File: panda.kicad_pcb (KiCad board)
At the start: 2 copper layers, 100 x 125 mm, 192 parts, among them J1 PIN10-13_Breakout, J10 XT60-M, J11 24V_Lockout_Key_Switch, J12 PT_1, J13 PT_4, J14 PT_2, J15 PT_5, J16 PT_3, J17 PT_6, J18 4-Pin Load Cell, J19 5-Pin Load Cell, J20 Ignitor Screw Terminal, J21 Screw_Terminal_01x03, J22 Screw_Terminal_01x02, J3 USB_C_Receptacle_USB2.0_16P, J4 Valve_1_PWR, J5 Valve_4_PWR, J6 Valve_2_PWR, J7 Valve_5_PWR, J8 Valve_3_PWR, J9 Valve_6_PWR, K1 G5Q-1A DC24, K2 G5Q-1A DC24, Q1 BSS138, Q2 BSS138, Q3 BSS138, Q4 BSS138, Q5 BSS138, Q6 BSS138, Q7 BSS138, Q8 BSS138, SW1 PTS636SM43SMTR LFS, SW2 PTS636SM43SMTR LFS, U1 ESP32-S3-WROOM-1, U2 ADS112C04, U3 ADS112C04, U4 ADS112C04, U5 ADS112C04, U6 TPS5430DDA, U7 XC6220B331PR-G, U8 INA187A1

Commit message: Update date
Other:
- board text added: "PANDA Propulsion Actuation and Nominal Data Acquisition V2.0.0 Nov 6th 2025 Noah Warren"
- board text removed: "PANDA Propulsion Actuation and Nominal Data Acquisition V1.1.0 Sep 10 2025 Noah Warren"
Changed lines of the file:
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@@
 			(psa4output no)
 			(plot_black_and_white yes)
+			(plotinvisibletext no)
 			(sketchpadsonfab no)
 			(plotpadnumbers no)
@@
 		)
 	)
-	(gr_text "PANDA\nPropulsion Actuation and Nominal Data Acquisition\nV1.1.0\nSep 10 2025\nNoah Warren"
+	(gr_text "PANDA\nPropulsion Actuation and Nominal Data Acquisition\nV2.0.0\nNov 6th 2025\nNoah Warren"
 		(at 69.75 151.5 0)
 		(layer "F.SilkS")

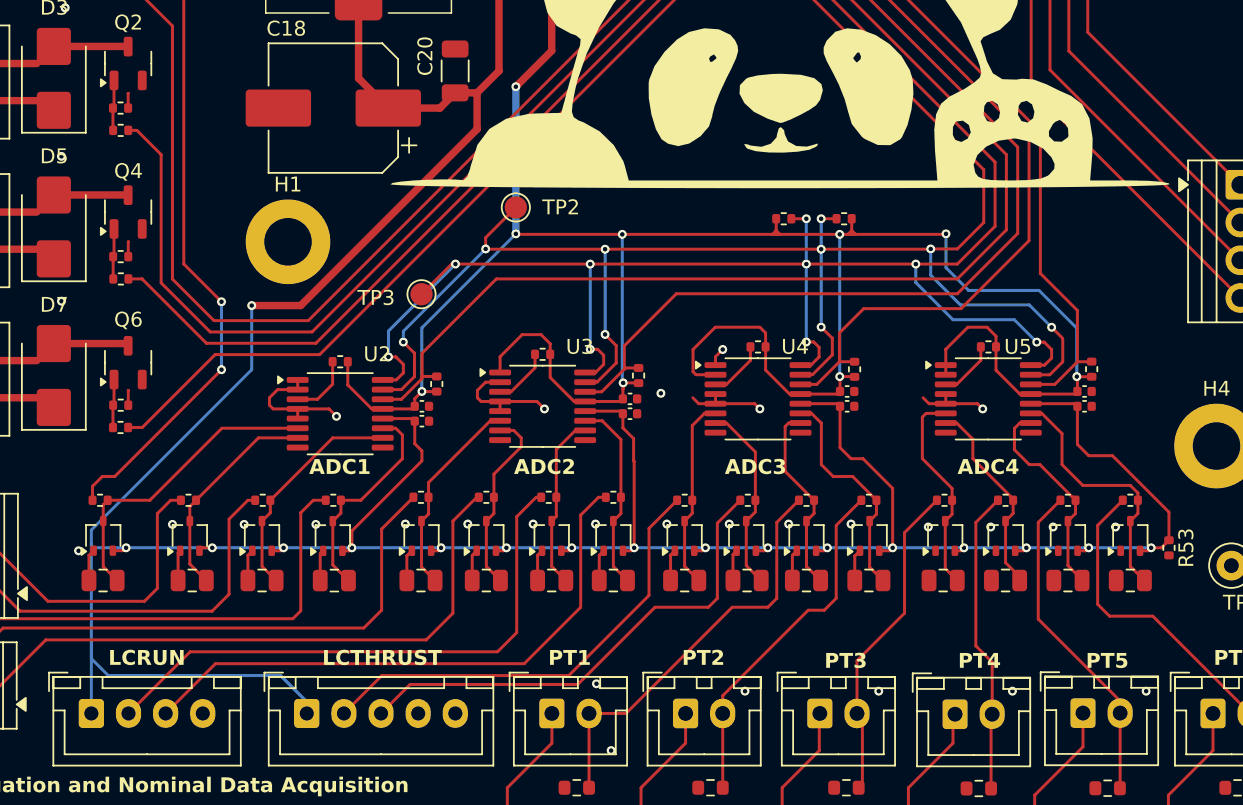
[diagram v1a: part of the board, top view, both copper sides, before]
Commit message: minor fixed + lowered status leds to ~0.6mA, which should give ~50 mcd
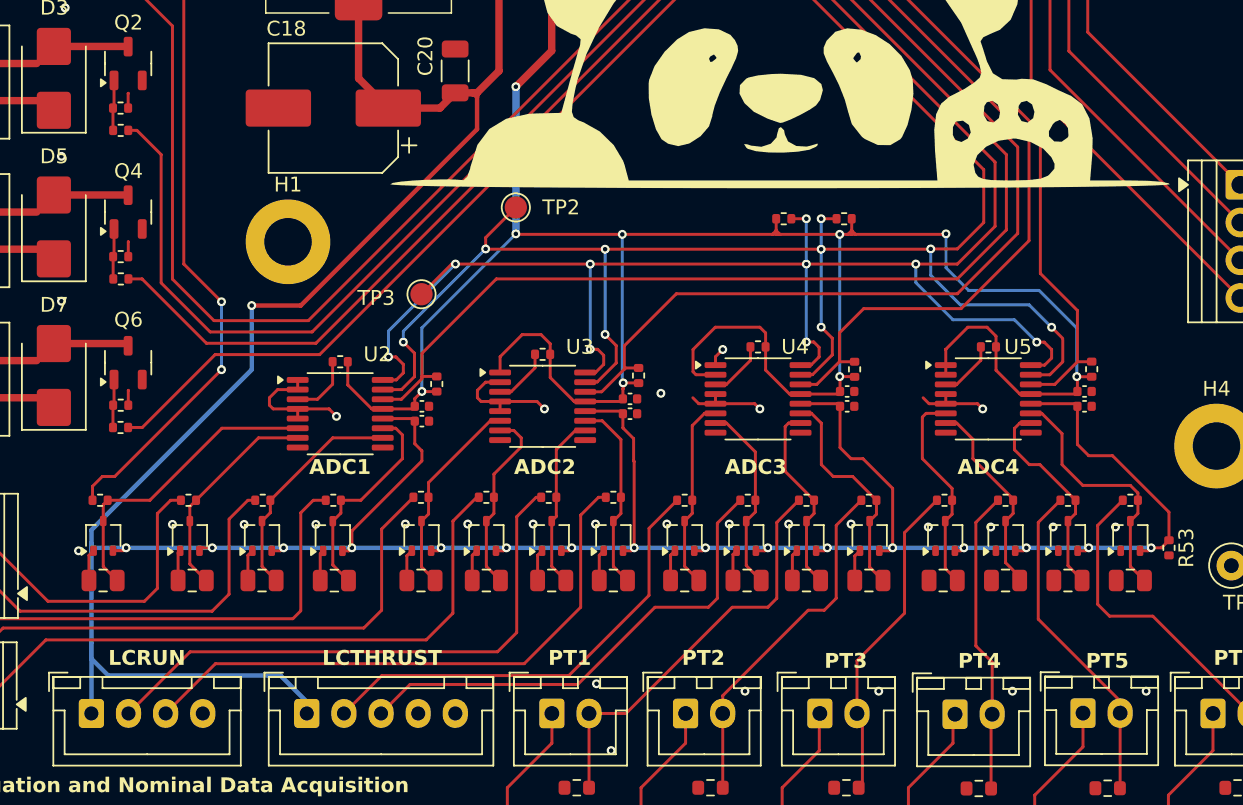
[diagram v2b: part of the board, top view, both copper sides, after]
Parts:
- R29, R32, R33, R50: value 22k -> 39k
- R40: value 1k -> 3.3k
- R8: value 33k -> 39k
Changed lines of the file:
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@@
 			)
 		)
-		(property "Value" "22k"
+		(property "Value" "39k"
 			(at 0 1.17 90)
 			(layer "F.Fab")
@@
 			)
 		)
-		(property "Value" "1k"
+		(property "Value" "3.3k"
 			(at 0 1.17 90)
 			(layer "F.Fab")
@@
 			)
 		)
-		(property "Value" "22k"
+		(property "Value" "39k"
 			(at 0 1.17 90)
 			(layer "F.Fab")
@@
 			)
 		)
-		(property "Value" "22k"
+		(property "Value" "39k"
 			(at 0 1.17 90)
 			(layer "F.Fab")
@@
 			)
 		)
-		(property "Value" "22k"
+		(property "Value" "39k"
 			(at 0 1.17 90)
 			(layer "F.Fab")
@@
 			)
 		)
-		(property "Value" "33k"
+		(property "Value" "39k"
 			(at 0 1.17 0)
 			(layer "F.Fab")
@@
 	)
 	(segment
-		(start 112.5 99.475)
+		(start 113.7 99.475)
 		(end 113.975 99.475)
 		(width 0.5)
@@
 	)
 	(segment
+		(start 112.5 99.475)
+		(end 113.7 99.475)
+		(width 0.5)
+		(layer "F.Cu")
+		(net 3)
+	)
+	(segment
 		(start 105.344221 130.305779)
 		(end 105.55 130.1)
@@
 		(start 102.108 113.792)
 		(end 98.806 113.792)
-		(width 0.5)
+		(width 0.3)
 		(layer "F.Cu")
 		(net 3)
@@
 		(start 113.975 101.925)
 		(end 102.108 113.792)
-		(width 0.5)
+		(width 0.3)
 		(layer "F.Cu")
 		(net 3)
@@
 	)
 	(segment
+		(start 113.975 99.75)
+		(end 113.975 101.925)
+		(width 0.3)
+		(layer "F.Cu")
+		(net 3)
+	)
+	(segment
 		(start 132.5 58.5)
 		(end 132.5 43.141)
@@
 	)
 	(segment
+		(start 113.975 99.75)
+		(end 113.7 99.475)
+		(width 0.3)
+		(layer "F.Cu")
+		(net 3)
+	)
+	(segment
 		(start 158.6 130.3)
 		(end 159.15 130.3)
@@
 	(segment
 		(start 113.975 99.475)
-		(end 113.975 101.925)
-		(width 0.5)
+		(end 113.975 99.75)
+		(width 0.3)
 		(layer "F.Cu")
 		(net 3)
@@
 		(start 100.95 130.1)
 		(end 105.55 130.1)
-		(width 0.2)
+		(width 0.3)
 		(layer "B.Cu")
 		(net 3)
@@
 		(start 88.012501 130.1)
 		(end 88.012501 129.794)
-		(width 0.2)
+		(width 0.3)
 		(layer "B.Cu")
 		(net 3)
@@
 		(start 105.55 130.1)
 		(end 111.55 130.1)
-		(width 0.2)
+		(width 0.3)
 		(layer "B.Cu")
 		(net 3)
@@
 		(start 137.55 130.1)
 		(end 141.95 130.1)
-		(width 0.2)
+		(width 0.3)
 		(layer "B.Cu")
 		(net 3)
@@
 		(start 100.75 138.7)
 		(end 89.15 138.7)
-		(width 0.2)
+		(width 0.3)
 		(layer "B.Cu")
 		(net 3)
@@
 		(start 141.95 130.1)
 		(end 146.75 130.1)
-		(width 0.2)
+		(width 0.3)
 		(layer "B.Cu")
 		(net 3)
@@
 		(start 115.95 130.1)
 		(end 120.35 130.1)
-		(width 0.2)
+		(width 0.3)
 		(layer "B.Cu")
 		(net 3)
@@
 		(start 102.512501 140.462501)
 		(end 100.75 138.7)
-		(width 0.2)
+		(width 0.3)
 		(layer "B.Cu")
 		(net 3)
@@
 		(start 133.55 130.1)
 		(end 137.55 130.1)
-		(width 0.2)
+		(width 0.3)
 		(layer "B.Cu")
 		(net 3)
@@
 		(start 88.012501 129.794)
 		(end 88.012501 129.974501)
-		(width 0.2)
+		(width 0.3)
 		(layer "B.Cu")
 		(net 3)
@@
 		(start 98.806 113.792)
 		(end 98.806 118.11)
-		(width 0.2)
+		(width 0.3)
 		(layer "B.Cu")
 		(net 3)
@@
 		(start 88.012501 136.5)
 		(end 88.012501 141.25)
-		(width 0.2)
+		(width 0.3)
 		(layer "B.Cu")
 		(net 3)
@@
 		(start 90.35 130.1)
 		(end 96.15 130.1)
-		(width 0.2)
+		(width 0.3)
 		(layer "B.Cu")
 		(net 3)
@@
 		(start 150.95 130.1)
 		(end 155.15 130.1)
-		(width 0.2)
+		(width 0.3)
 		(layer "B.Cu")
 		(net 3)
@@
 		(start 96.15 130.1)
 		(end 100.95 130.1)
-		(width 0.2)
+		(width 0.3)
 		(layer "B.Cu")
 		(net 3)
@@
 		(start 88.012501 130.1)
 		(end 88.138 130.1)
-		(width 0.2)
+		(width 0.3)
 		(layer "B.Cu")
 		(net 3)
@@
 		(start 88.012501 128.903499)
 		(end 88.012501 129.794)
-		(width 0.2)
+		(width 0.3)
 		(layer "B.Cu")
 		(net 3)
@@
 		(start 98.806 118.11)
 		(end 88.012501 128.903499)
-		(width 0.2)
+		(width 0.3)
 		(layer "B.Cu")
 		(net 3)
@@
 		(start 89.15 138.7)
 		(end 88.012501 137.562501)
-		(width 0.2)
+		(width 0.3)
 		(layer "B.Cu")
 		(net 3)
@@
 		(start 88.138 130.1)
 		(end 90.35 130.1)
-		(width 0.2)
+		(width 0.3)
 		(layer "B.Cu")
 		(net 3)
@@
 		(start 146.75 130.1)
 		(end 150.95 130.1)
-		(width 0.2)
+		(width 0.3)
 		(layer "B.Cu")
 		(net 3)
@@
 		(start 129.35 130.1)
 		(end 133.55 130.1)
-		(width 0.2)
+		(width 0.3)
 		(layer "B.Cu")
 		(net 3)
@@
 		(start 88.012501 130.1)
 		(end 88.012501 130.302)
-		(width 0.2)
+		(width 0.3)
 		(layer "B.Cu")
 		(net 3)
@@
 		(start 111.55 130.1)
 		(end 115.95 130.1)
-		(width 0.2)
+		(width 0.3)
 		(layer "B.Cu")
 		(net 3)
@@
 		(start 124.55 130.1)
 		(end 129.35 130.1)
-		(width 0.2)
+		(width 0.3)
 		(layer "B.Cu")
 		(net 3)
@@
 		(start 120.35 130.1)
 		(end 124.55 130.1)
-		(width 0.2)
+		(width 0.3)
 		(layer "B.Cu")
 		(net 3)
@@
 		(start 88.012501 130.302)
 		(end 88.012501 136.5)
-		(width 0.2)
+		(width 0.3)
 		(layer "B.Cu")
 		(net 3)
@@
 		(start 88.012501 129.974501)
 		(end 88.138 130.1)
-		(width 0.2)
+		(width 0.3)
 		(layer "B.Cu")
 		(net 3)
@@
 		(start 155.15 130.1)
 		(end 159.35 130.1)
-		(width 0.2)
+		(width 0.3)
 		(layer "B.Cu")
 		(net 3)

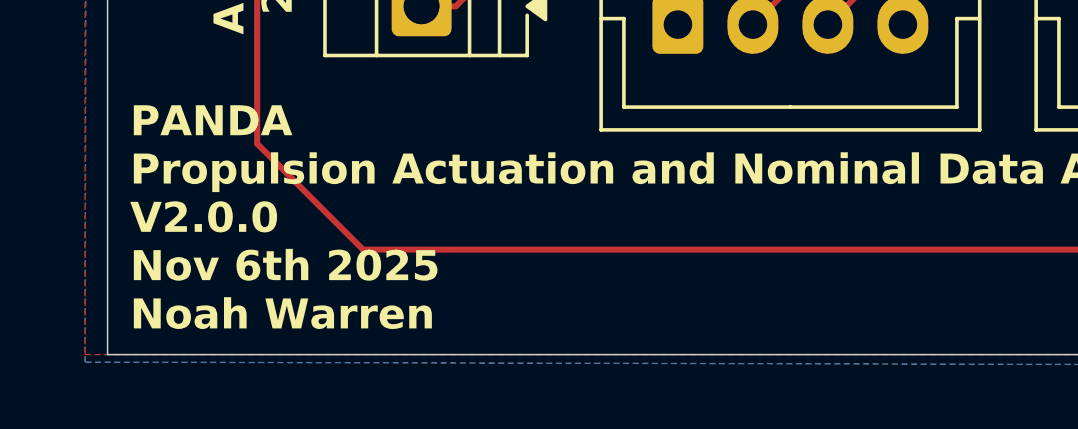
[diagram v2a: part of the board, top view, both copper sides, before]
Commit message: updated name on pcb
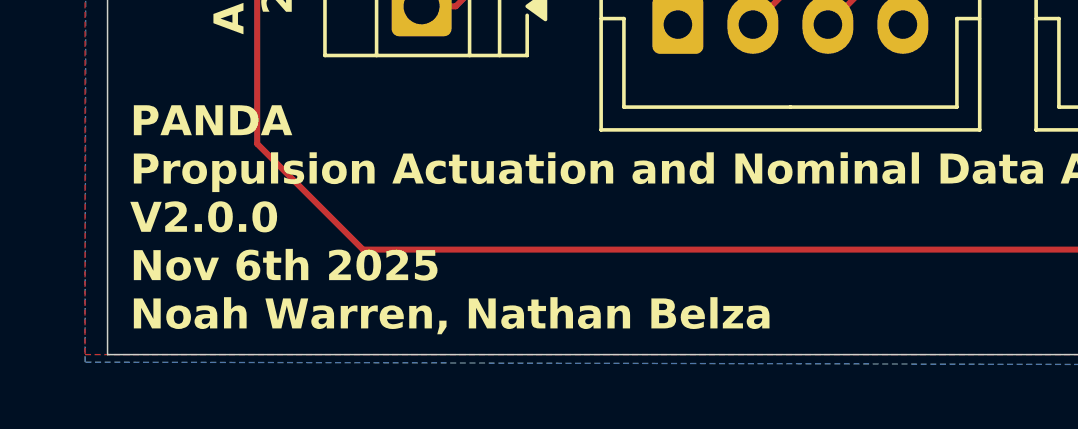
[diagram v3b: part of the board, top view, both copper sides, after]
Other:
- board text added: "PANDA Propulsion Actuation and Nominal Data Acquisition V2.0.0 Nov 6th 2025 Noah Warren, Nathan Belza"
- board text removed: "PANDA Propulsion Actuation and Nominal Data Acquisition V2.0.0 Nov 6th 2025 Noah Warren"
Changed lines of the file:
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@@
 			(psa4output no)
 			(plot_black_and_white yes)
-			(plotinvisibletext no)
 			(sketchpadsonfab no)
 			(plotpadnumbers no)
@@
 		)
 	)
-	(gr_text "PANDA\nPropulsion Actuation and Nominal Data Acquisition\nV2.0.0\nNov 6th 2025\nNoah Warren"
+	(gr_text "PANDA\nPropulsion Actuation and Nominal Data Acquisition\nV2.0.0\nNov 6th 2025\nNoah Warren, Nathan Belza"
 		(at 69.75 151.5 0)
 		(layer "F.SilkS")

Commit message: add capacitor and resistor footprints
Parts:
- removed G***: LOGO, LOGO
- removed J20: Ignitor Screw Terminal, TerminalBlock_4Ucon:TerminalBlock_4Ucon_1x02_P3.50mm_Vertical
- removed J21: Screw_Terminal_01x03, TerminalBlock:TerminalBlock_Xinya_XY308-2.54-3P_1x03_P2.54mm_Horizontal
- removed J22: Screw_Terminal_01x02, TerminalBlock:TerminalBlock_Xinya_XY308-2.54-2P_1x02_P2.54mm_Horizontal
- added C22: 22uF, Capacitor_SMD:C_0805_2012Metric, F.Cu at (100.3, 149.2)
- added C23: 0.1μF, Capacitor_SMD:C_0402_1005Metric, F.Cu at (96.6, 144.1)
- added C40: 0.1μF, Capacitor_SMD:C_0402_1005Metric, F.Cu at (88.6, 167.4)
- added C41: 10nF, Capacitor_SMD:C_0603_1608Metric, F.Cu at (89.1, 155.6)
- added C42: 0.1μF, Capacitor_SMD:C_0402_1005Metric, F.Cu at (159.7, 90.9)
- added C43: 10nF, Capacitor_SMD:C_0603_1608Metric, F.Cu at (89.1, 158.1)
- added C44: 10nF, Capacitor_SMD:C_0603_1608Metric, F.Cu at (89.1, 160.7)
- added C45: 0.1μF, Capacitor_SMD:C_0402_1005Metric, F.Cu at (159.7, 92.9)
- added C46: 10nF, Capacitor_SMD:C_0603_1608Metric, F.Cu at (89.1, 163.2)
- added C47: 0.1μF, Capacitor_SMD:C_0402_1005Metric, F.Cu at (69.0, 165.4)
- added C48: 0.1μF, Capacitor_SMD:C_0402_1005Metric, F.Cu at (69.0, 167.4)
- added C49: 10nF, Capacitor_SMD:C_0603_1608Metric, F.Cu at (69.5, 155.6)
- added C50: 0.1μF, Capacitor_SMD:C_0402_1005Metric, F.Cu at (154.8, 90.9)
- added C51: 10nF, Capacitor_SMD:C_0603_1608Metric, F.Cu at (69.5, 158.1)
- added C52: 10nF, Capacitor_SMD:C_0603_1608Metric, F.Cu at (69.5, 160.7)
- added C53: 0.1μF, Capacitor_SMD:C_0402_1005Metric, F.Cu at (154.8, 92.9)
- added C54: 10nF, Capacitor_SMD:C_0603_1608Metric, F.Cu at (69.5, 163.2)
- added C55: 3.3uF, Capacitor_SMD:C_0805_2012Metric, F.Cu at (33.9, 138.1)
- added C56: 3.3uF, Capacitor_SMD:C_0805_2012Metric, F.Cu at (33.9, 141.1)
- added C57: 3.3uF, Capacitor_SMD:C_0805_2012Metric, F.Cu at (33.9, 144.1)
- added C58: 3.3uF, Capacitor_SMD:C_0805_2012Metric, F.Cu at (33.9, 147.1)
- added C59: 3.3uF, Capacitor_SMD:C_0805_2012Metric, F.Cu at (33.9, 150.1)
- added C60: 3.3uF, Capacitor_SMD:C_0805_2012Metric, F.Cu at (33.9, 153.1)
- added C61: 0.1μF, Capacitor_SMD:C_0402_1005Metric, F.Cu at (98.8, 117.4)
- added C62: 0.1μF, Capacitor_SMD:C_0402_1005Metric, F.Cu at (108.1, 173.9)
- added C63: 0.1μF, Capacitor_SMD:C_0402_1005Metric, F.Cu at (108.1, 175.9)
- added C64: 150nF, Capacitor_SMD:C_0402_1005Metric, F.Cu at (108.1, 177.8)
- added C65: 150nF, Capacitor_SMD:C_0402_1005Metric, F.Cu at (108.1, 179.8)
- added C66: 150nF, Capacitor_SMD:C_0402_1005Metric, F.Cu at (108.1, 181.8)
- added C67: 150nF, Capacitor_SMD:C_0402_1005Metric, F.Cu at (108.1, 183.8)
- added D17: BAT54SW, Package_TO_SOT_SMD:SOT-323_SC-70, F.Cu at (84.9, 156.4)
- added D18: BAT54SW, Package_TO_SOT_SMD:SOT-323_SC-70, F.Cu at (84.9, 160.3)
- added D37: BAT54SW, Package_TO_SOT_SMD:SOT-323_SC-70, F.Cu at (104.5, 186.5)
- added F2: Fuse, Fuse:Fuseholder_Blade_Mini_Keystone_3568, F.Cu at (78.4, 112.3)
- added J2: XT60-M, Connector_AMASS:AMASS_XT60PW-F_1x02_P7.20mm_Horizontal, F.Cu at (34.6, 101.1)
- added K3: G5Q-1 DC24, Relay_THT:Relay_SPDT_Omron-G5Q-1, F.Cu at (77.1, 107.4)
- added Q10: BSS138, Package_TO_SOT_SMD:SOT-23-3, F.Cu at (58.5, 156.6)
- added Q11: BSS138, Package_TO_SOT_SMD:SOT-23-3, F.Cu at (58.5, 161.1)
- added Q9: BSS138, Package_TO_SOT_SMD:SOT-23-3, F.Cu at (58.5, 152.2)
- added R47: Rb, Resistor_SMD:R_0402_1005Metric, F.Cu at (92.6, 164.0)
- added R48: Rb, Resistor_SMD:R_0402_1005Metric, F.Cu at (92.6, 165.9)
- added R70: 250, Resistor_SMD:R_0603_1608Metric, F.Cu at (33.6, 160.9)
- added R71: 250, Resistor_SMD:R_0603_1608Metric, F.Cu at (33.6, 163.4)
- added R72: 10, Resistor_SMD:R_0402_1005Metric, F.Cu at (125.4, 161.1)
- added R73: 10, Resistor_SMD:R_0402_1005Metric, F.Cu at (125.4, 163.1)
- added R74: 250, Resistor_SMD:R_0603_1608Metric, F.Cu at (33.6, 165.9)
- added R75: 250, Resistor_SMD:R_0603_1608Metric, F.Cu at (33.6, 168.4)
- added R76: 39k, Resistor_SMD:R_0402_1005Metric, F.Cu at (98.8, 107.5)
- added R77: 25m 1W, Resistor_SMD:R_1206_3216Metric, F.Cu at (103.0, 117.0)
- added R78: 10k, Resistor_SMD:R_0402_1005Metric, F.Cu at (98.8, 109.4)
- added R79: 10k, Resistor_SMD:R_0402_1005Metric, F.Cu at (98.8, 111.4)
- added R80: 100, Resistor_SMD:R_0402_1005Metric, F.Cu at (98.8, 113.4)
- added R81: 100, Resistor_SMD:R_0402_1005Metric, F.Cu at (98.8, 115.4)
- added R82: 100, Resistor_SMD:R_0402_1005Metric, F.Cu at (49.0, 170.9)
- added R83: 100, Resistor_SMD:R_0402_1005Metric, F.Cu at (49.0, 172.9)
- added R84: 100k, Resistor_SMD:R_0603_1608Metric, F.Cu at (49.0, 174.8)
- added R85: 100k, Resistor_SMD:R_0603_1608Metric, F.Cu at (49.0, 176.8)
- added R86: 100, Resistor_SMD:R_0402_1005Metric, F.Cu at (51.9, 170.9)
- added R87: 100, Resistor_SMD:R_0402_1005Metric, F.Cu at (51.9, 172.9)
- added R88: 100k, Resistor_SMD:R_0603_1608Metric, F.Cu at (51.9, 174.8)
- added R89: 100k, Resistor_SMD:R_0603_1608Metric, F.Cu at (51.9, 176.8)
- added R90: 100, Resistor_SMD:R_0402_1005Metric, F.Cu at (54.8, 170.9)
- added R91: 100, Resistor_SMD:R_0402_1005Metric, F.Cu at (54.8, 172.9)
- added R92: 100k, Resistor_SMD:R_0603_1608Metric, F.Cu at (54.8, 174.8)
- added R93: 100k, Resistor_SMD:R_0603_1608Metric, F.Cu at (54.8, 176.8)
- added R94: 47, Resistor_SMD:R_0402_1005Metric, F.Cu at (111.0, 173.9)
- added R95: 1k, Resistor_SMD:R_0402_1005Metric, F.Cu at (111.0, 175.9)
- added R96: 1k, Resistor_SMD:R_0402_1005Metric, F.Cu at (111.0, 177.9)
- added R97: 1k, Resistor_SMD:R_0402_1005Metric, F.Cu at (111.0, 179.9)
- added R98: 10k, Resistor_SMD:R_0402_1005Metric, F.Cu at (111.0, 181.9)
- added U10: ADS112C04, Package_SO:TSSOP-16_4.4x5mm_P0.65mm, F.Cu at (95.9, 157.7)
- added U11: ADS112C04, Package_SO:TSSOP-16_4.4x5mm_P0.65mm, F.Cu at (76.3, 157.7)
- added U12: INA187A1, Package_TO_SOT_SMD:SOT-23-6, F.Cu at (94.8, 112.2)
- added U13: ADS112C04, Package_SO:TSSOP-16_4.4x5mm_P0.65mm, F.Cu at (114.3, 186.2)
- added U9: ADS112C04, Package_SO:TSSOP-16_4.4x5mm_P0.65mm, F.Cu at (115.5, 105.2)
- C1: value 22uF -> 0.1μF; footprint Capacitor_SMD:C_1206_3216Metric -> Capacitor_SMD:C_0402_1005Metric
- C10, C12: value 0.1μF -> 22uF; footprint Capacitor_SMD:C_0402_1005Metric -> Capacitor_SMD:C_0805_2012Metric
- C11: value 0.1μF -> 10nF
- C13, C8: value 0.1μF -> 10uF; footprint Capacitor_SMD:C_0402_1005Metric -> Capacitor_SMD:C_0805_2012Metric
- C14, C15: value 10uF -> 0.1μF; footprint Capacitor_SMD:C_1206_3216Metric -> Capacitor_SMD:C_0402_1005Metric
- C16: value 10nF -> 2.2uF; footprint Capacitor_SMD:C_0402_1005Metric -> Capacitor_SMD:C_0603_1608Metric
- C17, C20: footprint Capacitor_SMD:C_1206_3216Metric -> Capacitor_SMD:C_0805_2012Metric
- C18: value 220uF -> 0.1μF; footprint Capacitor_SMD:CP_Elec_8x10.5 -> Capacitor_SMD:C_0402_1005Metric
- C2: value 0.1μF -> 100uF; footprint Capacitor_SMD:C_0402_1005Metric -> Capacitor_SMD:CP_Elec_10x10
- C24: value 68nF -> 1uF; footprint Capacitor_SMD:C_0805_2012Metric -> Capacitor_SMD:C_0603_1608Metric
- C25, C26, C27, C28, C33, C34, C39: value 68nF -> 0.1μF; footprint Capacitor_SMD:C_0805_2012Metric -> Capacitor_SMD:C_0402_1005Metric
- C29, C30, C31, C32, C35, C36, C37, C38: value 68nF -> 150nF; footprint Capacitor_SMD:C_0805_2012Metric -> Capacitor_SMD:C_0402_1005Metric
- C3: value 0.1μF -> 10uF; footprint Capacitor_SMD:C_0402_1005Metric -> Capacitor_SMD:C_1206_3216Metric
- C4: value 1μF -> 10uF; footprint Capacitor_SMD:C_0402_1005Metric -> Capacitor_SMD:C_1206_3216Metric
- C5: value 0.1uF -> 220nF; footprint Capacitor_SMD:C_0402_1005Metric -> Capacitor_SMD:C_0805_2012Metric
- C6: value 0.1μF -> 1uF; footprint Capacitor_SMD:C_0402_1005Metric -> Capacitor_SMD:C_0603_1608Metric
- C9: value 0.1μF -> 3pF; footprint Capacitor_SMD:C_0402_1005Metric -> Capacitor_SMD:C_0603_1608Metric
- D1: value LED-Y -> LED-G
- D10, D15, D16, D19, D9: value LED-G -> BAT54SW; footprint LED_SMD:LED_0805_2012Metric -> Package_TO_SOT_SMD:SOT-323_SC-70
- D11, D14, D20: value SK44BL -> BAT54SW; footprint Diode_SMD:D_SMB -> Package_TO_SOT_SMD:SOT-323_SC-70
- D12, D13: value 1N5819HW-7-F -> BAT54SW; footprint Diode_SMD:D_SOD-123 -> Package_TO_SOT_SMD:SOT-323_SC-70
- D2: value SK44BL -> SMCJ26A-13-F; footprint Diode_SMD:D_SMB -> Diode_SMD:D_SMC
- D25: value BAT54SW -> LED-G; footprint Package_TO_SOT_SMD:SOT-323_SC-70 -> LED_SMD:LED_0805_2012Metric
- D26, D27, D28, D29, D30, D31, D32, D33: value BAT54SW -> SK44BL; footprint Package_TO_SOT_SMD:SOT-323_SC-70 -> Diode_SMD:D_SMB
- D3, D4, D6, D7: value SK44BL -> LED-G; footprint Diode_SMD:D_SMB -> LED_SMD:LED_0805_2012Metric
- D8: value LED-G -> LED-Y
- J1: value PIN10-13_Breakout -> Logic_Power_Switch; footprint TerminalBlock:TerminalBlock_Xinya_XY308-2.54-4P_1x04_P2.54mm_Horizontal -> Connector_JST:JST_XH_B2B-XH-A_1x02_P2.50mm_Vertical
- J10: value XT60-M -> PT_6; footprint Connector_AMASS:AMASS_XT60PW-F_1x02_P7.20mm_Horizontal -> Connector_JST:JST_XH_B2B-XH-A_1x02_P2.50mm_Vertical
- J11: value 24V_Lockout_Key_Switch -> 4-Pin Load Cell; footprint Connector_JST:JST_XH_B2B-XH-A_1x02_P2.50mm_Vertical -> Connector_JST:JST_XH_B4B-XH-A_1x04_P2.50mm_Vertical
- J12: value PT_1 -> 5-Pin Load Cell; footprint Connector_JST:JST_XH_B2B-XH-A_1x02_P2.50mm_Vertical -> Connector_JST:JST_XH_B5B-XH-A_1x05_P2.50mm_Vertical
- J13: value PT_4 -> Ignitor Screw Terminal; footprint Connector_JST:JST_XH_B2B-XH-A_1x02_P2.50mm_Vertical -> TerminalBlock_4Ucon:TerminalBlock_4Ucon_1x02_P3.50mm_Vertical
- J14: value PT_2 -> Valve_1_PWR
- J15: value PT_5 -> Valve_4_PWR
- J16: value PT_3 -> Valve_2_PWR
- J17: value PT_6 -> Valve_5_PWR
- J18: value 4-Pin Load Cell -> Valve_3_PWR; footprint Connector_JST:JST_XH_B4B-XH-A_1x04_P2.50mm_Vertical -> Connector_JST:JST_XH_B2B-XH-A_1x02_P2.50mm_Vertical
- J19: value 5-Pin Load Cell -> Valve_6_PWR; footprint Connector_JST:JST_XH_B5B-XH-A_1x05_P2.50mm_Vertical -> Connector_JST:JST_XH_B2B-XH-A_1x02_P2.50mm_Vertical
- J3: value USB_C_Receptacle_USB2.0_16P -> 24V_Lockout_Key_Switch; footprint Connector_USB:USB_C_Receptacle_HCTL_HC-TYPE-C-16P-01A -> Connector_JST:JST_XH_B2B-XH-A_1x02_P2.50mm_Vertical
- J4: value Valve_1_PWR -> USB_C_Receptacle_USB2.0_16P; footprint Connector_JST:JST_XH_B2B-XH-A_1x02_P2.50mm_Vertical -> Connector_USB:USB_C_Receptacle_G-Switch_GT-USB-7010ASV
- J5: value Valve_4_PWR -> PT_1
- J6: value Valve_2_PWR -> PT_4
- J7: value Valve_5_PWR -> PT_2
- J8: value Valve_3_PWR -> PT_5
- J9: value Valve_6_PWR -> PT_3
- K2: value G5Q-1A DC24 -> G5Q-1 DC24; footprint Relay_THT:Relay_SPST_Omron-G5Q-1A -> Relay_THT:Relay_SPDT_Omron-G5Q-1
- L1: value 22uH 4A -> 4.7uH; footprint Inductor_SMD:L_12.5x12.5mm_SXNSMDRS1275 -> Inductor_SMD:L_Bourns_SRP7028A_7.3x6.6mm
- Q3: value BSS138 -> DMP6023LE-13; footprint Package_TO_SOT_SMD:SOT-23-3 -> Package_TO_SOT_SMD:SOT-223-3_TabPin2
- R1: value 10k -> 3.3k
- R10, R14: value 100 -> 100k; footprint Resistor_SMD:R_0402_1005Metric -> Resistor_SMD:R_0603_1608Metric
- R11: value 100k -> 39k
- R12, R20: footprint Resistor_SMD:R_0402_1005Metric -> Resistor_SMD:R_0603_1608Metric
- R13, R35, R9: value 100 -> 39k
- R15, R19, R30: value 100k -> 10k
- R16: value 100k -> 100
- R17: value 100 -> 470k; footprint Resistor_SMD:R_0402_1005Metric -> Resistor_SMD:R_0603_1608Metric
- R18: value 100 -> 10k
- R2, R3: value 1k -> 3.3k
- R21: value 10k -> 100k; footprint Resistor_SMD:R_0402_1005Metric -> Resistor_SMD:R_0603_1608Metric
- R22: value 10k -> 23.2k; footprint Resistor_SMD:R_0402_1005Metric -> Resistor_SMD:R_0603_1608Metric
- R23, R28: value 3.3k -> 100k; footprint Resistor_SMD:R_0402_1005Metric -> Resistor_SMD:R_0603_1608Metric
- R24: value 3.3k -> 18k; footprint Resistor_SMD:R_0402_1005Metric -> Resistor_SMD:R_0603_1608Metric
- R25: value 10k -> 1.2k
- R26: value 10k -> 160k
- R27, R40: value 3.3k -> 10k
- R29: value 39k -> 3.3k
- R31, R38, R51, R53: value 10k -> 1k
- R32, R33: value 39k -> 5.1k
- R34: value 10k -> 270k
- R36: value 100k -> 1k
- R37: value 680 -> 1k
- R39: value 3.3k -> 1k
- R4, R5: value 5.1k -> 3.3k
- R41, R42, R43, R44: value 250R -> 1k; footprint Resistor_SMD:R_0603_1608Metric -> Resistor_SMD:R_0402_1005Metric
- R45, R46: value 250R -> 10k; footprint Resistor_SMD:R_0603_1608Metric -> Resistor_SMD:R_0402_1005Metric
- R49: value 25m 1W -> Rb; footprint Resistor_SMD:R_1206_3216Metric -> Resistor_SMD:R_0402_1005Metric
- R50: value 39k -> Rb
- R52: value 100 -> 1k
- R54, R60, R61, R62, R63: value 2.2k -> 1k
- R55: value 2.2k -> 10k
- R56, R57, R58, R59: value 2.2k -> Rb
- R64, R65, R68, R69: value 2.2k -> 10
- R66, R67: value 2.2k -> 250; footprint Resistor_SMD:R_0402_1005Metric -> Resistor_SMD:R_0603_1608Metric
- R7: value 270k -> 1k
- R8: value 39k -> 100k; footprint Resistor_SMD:R_0402_1005Metric -> Resistor_SMD:R_0603_1608Metric
- SW1, SW2: value PTS636SM43SMTR LFS -> USAKRO UK-B0227-G4.3-B-250
- U1: value ESP32-S3-WROOM-1 -> LM3880-1AA; footprint RF_Module:ESP32-S3-WROOM-1 -> Package_TO_SOT_SMD:SOT-23-6
- U2: value ADS112C04 -> LMR33630BDDA; footprint Package_SO:TSSOP-16_4.4x5mm_P0.65mm -> Package_SO:Texas_HSOP-8-1EP_3.9x4.9mm_P1.27mm_ThermalVias
- U3: value ADS112C04 -> TPS78533QKVURQ1; footprint Package_SO:TSSOP-16_4.4x5mm_P0.65mm -> Package_TO_SOT_SMD:TO-252-4
- U4: value ADS112C04 -> TLC555xD; footprint Package_SO:TSSOP-16_4.4x5mm_P0.65mm -> Package_SO:SOIC-8_3.9x4.9mm_P1.27mm
- U5: value ADS112C04 -> TPS78450QDBVRQ1; footprint Package_SO:TSSOP-16_4.4x5mm_P0.65mm -> Package_TO_SOT_SMD:SOT-23-5
- U6: value TPS5430DDA -> LM66200DRLR; footprint Package_SO:TI_SO-PowerPAD-8_ThermalVias -> Package_TO_SOT_SMD:SOT-583-8
- U7: value XC6220B331PR-G -> ESP32-S3-WROOM-1U; footprint Package_TO_SOT_SMD:SOT-89-5 -> RF_Module:ESP32-S3-WROOM-1U
- U8: value INA187A1 -> ADS112C04; footprint Package_TO_SOT_SMD:SOT-23-6 -> Package_SO:TSSOP-16_4.4x5mm_P0.65mm
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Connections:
- C1 pad 1: +3.3V -> GND
- C1 pad 2: GND -> /Power Regulation/PWR_SQ
- C10 pad 1: +3.3V -> /Power Regulation/+5.3V
- C11 pad 1: +3.3V -> GND
- C11 pad 2: GND -> Net-(U4-CV)
- C12 pad 1: +5V -> /Power Regulation/+5.3V
- C13 pad 1: +5V -> +3.3V
- C14 pad 1: +24V -> GND
- C14 pad 2: GND -> /Power Regulation/+5.3V
- C15 pad 1: Net-(D12-K) -> GND
- C15 pad 2: GND -> /Power Regulation/+5.3V
- C16 pad 1: Net-(U6-BOOT) -> /Power Regulation/TR
- C16 pad 2: Net-(D14-K) -> GND
- C17 pad 1: +3.3V -> /Power Regulation/PWR_SQ
- C18 pad 1: +5V -> GND
- C18 pad 2: GND -> /Power Regulation/+5.3V
- C19 pad 1: +3.3V -> GND
- C19 pad 2: GND -> 5V_USB
- C2 pad 1: RESET -> +24V
- C21 pad 2: +5V -> /Power Regulation/PWR_SQ
- C24 pad 1: ADC1_AIN3 -> /ESP32 Breakout/RESET
- C25 pad 1: ADC1_AIN0 -> /ESP32 Breakout/RESET
- C26 pad 1: ADC2_AIN3 -> 5V_USB
- C27 pad 1: ADC2_AIN0 -> +3.3V
- C28 pad 1: ADC1_AIN2 -> +5V
- C29 pad 1: ADC1_AIN1 -> /ADC1/AIN3
- C3 pad 1: +3.3V -> +24V
- C30 pad 1: ADC2_AIN2 -> /ADC1/AIN0
- C31 pad 1: ADC2_AIN1 -> /ADC1/AIN2
- C32 pad 1: ADC3_AIN3 -> /ADC1/AIN1
- C33 pad 1: ADC3_AIN0 -> +3.3V
- C34 pad 1: ADC4_AIN3 -> +5V
- C35 pad 1: ADC4_AIN0 -> /ADC2/AIN3
- C36 pad 1: ADC3_AIN2 -> /ADC2/AIN0
- C37 pad 1: ADC3_AIN1 -> /ADC2/AIN2
- C38 pad 1: ADC4_AIN2 -> /ADC2/AIN1
- C39 pad 1: ADC4_AIN1 -> +3.3V
- C4 pad 1: RESET -> +24V
- C5 pad 1: 5V_USB -> +24V
- C6 pad 1: +3.3V -> /Power Regulation/VCC
- C7 pad 1: +3.3V -> Net-(U2-BOOT)
- C7 pad 2: GND -> /Power Regulation/SW
- C8 pad 1: +5V -> /Power Regulation/PWR_SQ
- C9 pad 1: +5V -> /Power Regulation/+5.3V
- C9 pad 2: GND -> Net-(U2-FB)
- CR1 pad 4: USB_P -> /ESP32 Breakout/USB_P
- CR1 pad 6: USB_N -> /ESP32 Breakout/USB_N
- D10 pad 2: Net-(D10-A) -> +5V
- D11 pad 1: +24V -> GND
- D11 pad 2: Net-(D11-A) -> +5V
- D12 pad 1: Net-(D12-K) -> GND
- D13 pad 1: Net-(D12-K) -> GND
- D13 pad 2: 5V_USB -> +5V
- D14 pad 1: Net-(D14-K) -> GND
- D14 pad 2: GND -> +5V
- D15 pad 2: Net-(D15-A) -> +5V
- D16 pad 2: Net-(D16-A) -> +5V
- D19 pad 2: Net-(D19-A) -> +5V
- D2 pad 1: +24V_SAFE -> +24V
- D2 pad 2: VALVE_1_RET -> GND
- D20 pad 1: +24V_SAFE -> GND
- D20 pad 2: Net-(D20-A) -> +5V
- D21 pad 3: ADC1_AIN3 -> TC3+
- D22 pad 3: ADC1_AIN0 -> TC3-
- D23 pad 3: ADC2_AIN3 -> TC4+
- D24 pad 3: ADC2_AIN0 -> TC4-
- D25 pad 2: +5V -> Net-(D25-A)
- D26 pad 1: GND -> +24V_SAFE
- D26 pad 2: +5V -> Net-(D26-A)
- D27 pad 1: GND -> +24V_SAFE
- D27 pad 2: +5V -> Net-(D27-A)
- D28 pad 1: GND -> +24V_SAFE
- D28 pad 2: +5V -> /Valve Control/VALVE_1_RET
- D29 pad 1: GND -> +24V
- D29 pad 2: +5V -> /Valve Control/VALVE_4_RET
- D3 pad 1: +24V -> GND
- D3 pad 2: VALVE_4_RET -> Net-(D3-A)
- D30 pad 1: GND -> +24V_SAFE
- D30 pad 2: +5V -> /Valve Control/VALVE_2_RET
- D31 pad 1: GND -> +24V
- D31 pad 2: +5V -> /Valve Control/VALVE_5_RET
- D32 pad 1: GND -> +24V
- D32 pad 2: +5V -> /Valve Control/VALVE_3_RET
- D33 pad 1: GND -> +24V
- D33 pad 2: +5V -> /Valve Control/VALVE_6_RET
- D34 pad 3: ADC3_AIN1 -> /IgnitorADC/AIN3
- D35 pad 3: ADC4_AIN2 -> /IgnitorADC/AIN0
- D36 pad 3: ADC4_AIN1 -> /IgnitorADC/AIN2
- D4 pad 1: +24V_SAFE -> GND
- D4 pad 2: VALVE_2_RET -> Net-(D4-A)
- D5 pad 2: VALVE_5_RET -> Net-(D5-A)
- D6 pad 1: +24V -> GND
- D6 pad 2: VALVE_3_RET -> Net-(D6-A)
- D7 pad 1: +24V -> GND
- D7 pad 2: VALVE_6_RET -> Net-(D7-A)
- D9 pad 2: Net-(D9-A) -> +5V
- F1 pad 1: /Ignitor Control/IGN_SUPPLY -> Net-(J2-POS)
- F1 pad 2: Net-(U8--) -> +24V
- J1 pad 1: MTMS -> Net-(J1-Pin_1)
- J1 pad 2: MTDI -> /Power Regulation/PWR_SQ
- J10 pad 1: +24V -> Net-(J10-Pin_1)
- J10 pad 2: GND -> PT_READ_6
- J11 pad 1: +24V -> +5V
- J11 pad 2: /Power Regulation/+24V_POST_LOCKOUT -> LC_FILL_+
- J12 pad 1: +24V -> +5V
- J12 pad 2: PT_READING_1 -> LC_THRUST_+
- J13 pad 1: +24V -> /Ignitor Control/IGNITOR_+VE
- J13 pad 2: PT_READING_4 -> GND
- J14 pad 1: +24V -> +24V_SAFE
- J14 pad 2: PT_READING_2 -> /Valve Control/VALVE_1_RET
- J15 pad 2: PT_READING_5 -> /Valve Control/VALVE_4_RET
- J16 pad 1: +24V -> +24V_SAFE
- J16 pad 2: PT_READING_3 -> /Valve Control/VALVE_2_RET
- J17 pad 2: PT_READING_6 -> /Valve Control/VALVE_5_RET
- J18 pad 1: +5V -> +24V
- J18 pad 2: LC_FILL_+ -> /Valve Control/VALVE_3_RET
- J19 pad 1: +5V -> +24V
- J19 pad 2: LC_THRUST_+ -> /Valve Control/VALVE_6_RET
- J5 pad 1: +24V -> Net-(J5-Pin_1)
- J5 pad 2: VALVE_4_RET -> PT_READ_1
- J6 pad 1: +24V_SAFE -> Net-(J6-Pin_1)
- J6 pad 2: VALVE_2_RET -> PT_READ_4
- J7 pad 1: +24V -> Net-(J7-Pin_1)
- J7 pad 2: VALVE_5_RET -> PT_READ_2
- J8 pad 1: +24V -> Net-(J8-Pin_1)
- J8 pad 2: VALVE_3_RET -> PT_READ_5
- J9 pad 1: +24V -> Net-(J9-Pin_1)
- J9 pad 2: VALVE_6_RET -> PT_READ_3
- K1 pad 1: +24V -> Net-(D5-A)
- K1 pad 2: /Power Regulation/+24V_POST_LOCKOUT -> +24V_SAFE
- K1 pad 3: +24V_SAFE -> /Power Regulation/+24V_POST_LCKT
- K1 pad 5: Net-(D11-A) -> +24V
- K2 pad 1: +24V_SAFE -> Net-(D26-A)
- K2 pad 2: +24V_SAFE -> Net-(U12-+)
- K2 pad 3: /Ignitor Control/IGN_SUPPLY -> +24V_SAFE
- K2 pad 5: Net-(D20-A) -> +24V_SAFE
- L1 pad 1: Net-(D14-K) -> /Power Regulation/SW
- L1 pad 2: +5V -> /Power Regulation/+5.3V
- Q1 pad 3: VALVE_1_RET -> Net-(D5-A)
- Q2 pad 3: VALVE_4_RET -> Net-(Q2-D)
- Q3 pad 2: GND -> +24V_PT
- Q3 pad 3: VALVE_2_RET -> +24V
- Q4 pad 3: VALVE_5_RET -> Net-(D27-A)
- Q5 pad 3: VALVE_3_RET -> Net-(D26-A)
- Q6 pad 3: VALVE_6_RET -> /Valve Control/VALVE_1_RET
- Q7 pad 1: /Power Regulation/LOCKOUT_RLY_CTRL_FET -> Net-(Q7-G)
- Q7 pad 3: Net-(D11-A) -> /Valve Control/VALVE_4_RET
- Q8 pad 1: /Ignitor Control/IGNITOR_CTL_FET -> Net-(Q8-G)
- Q8 pad 3: Net-(D20-A) -> /Valve Control/VALVE_2_RET
- R1 pad 1: RESET -> +3.3V
- R1 pad 2: +3.3V -> DRDY1
- R10 pad 1: VALVE_4_CTL -> /Power Regulation/+3.3V_EN
- R10 pad 2: Net-(Q2-G) -> /Power Regulation/PWR_SQ
- R11 pad 1: Net-(Q1-G) -> Net-(D3-A)
- R11 pad 2: GND -> +24V_SAFE
- R12 pad 1: Net-(Q2-G) -> /Power Regulation/+5V_EN
- R12 pad 2: GND -> /Power Regulation/PWR_SQ
- R13 pad 1: VALVE_2_CTL -> Net-(D4-A)
- R13 pad 2: Net-(Q3-G) -> +24V
- R14 pad 1: VALVE_5_CTL -> Net-(Q2-G)
- R14 pad 2: Net-(Q4-G) -> /Power Regulation/PWR_SQ
- R15 pad 1: Net-(Q3-G) -> Net-(Q1-G)
- R16 pad 1: Net-(Q4-G) -> Net-(Q1-G)
- R16 pad 2: GND -> SAFE_24V_CTL
- R17 pad 1: VALVE_3_CTL -> GND
- R17 pad 2: Net-(Q5-G) -> Net-(Q2-G)
- R18 pad 1: VALVE_6_CTL -> Net-(Q3-G)
- R18 pad 2: Net-(Q6-G) -> +24V
- R19 pad 1: Net-(Q5-G) -> Net-(Q2-D)
- R19 pad 2: GND -> Net-(Q3-G)
- R2 pad 2: I2C_SDA -> DRDY2
- R20 pad 1: Net-(Q6-G) -> BUCK_PG
- R20 pad 2: GND -> /Power Regulation/VCC
- R21 pad 1: +3.3V -> /Power Regulation/+5.3V
- R21 pad 2: Net-(U2-RESET) -> Net-(U2-FB)
- R22 pad 1: +3.3V -> Net-(U2-FB)
- R22 pad 2: Net-(U3-RESET) -> GND
- R23 pad 1: +3.3V -> Net-(U4-R)
- R23 pad 2: I2C_DRDY_ADC1 -> +24V_SAFE
- R24 pad 1: +3.3V -> GND
- R24 pad 2: I2C_DRDY_ADC2 -> Net-(U4-R)
- R25 pad 1: +3.3V -> Net-(D6-A)
- R25 pad 2: Net-(U4-RESET) -> +3.3V
- R26 pad 1: +3.3V -> Net-(U4-DIS)
- R26 pad 2: Net-(U5-RESET) -> /Power Regulation/TR
- R27 pad 1: +3.3V -> Net-(U4-DIS)
- R27 pad 2: I2C_DRDY_ADC4 -> /Power Regulation/+5.3V
- R28 pad 1: +3.3V -> Net-(U6-ST)
- R28 pad 2: I2C_DRDY_ADC3 -> /Power Regulation/PWR_SQ
- R29 pad 1: Net-(D8-A) -> Net-(D7-A)
- R29 pad 2: /Power Regulation/+24V_POST_LOCKOUT -> +5V
- R3 pad 2: I2C_SCL -> DRDY3
- R30 pad 1: +24V -> /ESP32 Breakout/RESET
- R30 pad 2: /Power Regulation/VREG_EN -> +3.3V
- R31 pad 1: /Power Regulation/VREG_EN -> Net-(D8-A)
- R31 pad 2: GND -> /ESP32 Breakout/WIFI_IND
- R32 pad 1: Net-(D9-A) -> Net-(J4-CC1)
- R32 pad 2: +24V -> GND
- R33 pad 1: Net-(D10-A) -> Net-(J4-CC2)
- R33 pad 2: +24V_SAFE -> GND
- R34 pad 1: /Power Regulation/LOCKOUT_RLY_CTRL_FET -> +24V_SAFE
- R34 pad 2: GND -> /ESP32 Breakout/24V_SAFE_DETECT
- R35 pad 1: /Power Regulation/LOCKOUT_RLY_CTRL_FET -> /ESP32 Breakout/24V_SAFE_DETECT
- R35 pad 2: SAFE_24V_CTL -> GND
- R36 pad 1: GND -> LC_THRUST_+
- R36 pad 2: 5V_USB -> /ADC1/AIN3
- R37 pad 1: Net-(D15-A) -> LC_THRUST_-
- R37 pad 2: +3.3V -> /ADC1/AIN2
- R38 pad 1: +5V -> LC_FILL_+
- R38 pad 2: Net-(U6-VSENSE) -> /ADC1/AIN1
- R39 pad 1: Net-(U6-VSENSE) -> LC_FILL_-
- R39 pad 2: GND -> /ADC1/AIN0
- R4 pad 1: Net-(J3-CC1) -> +3.3V
- R4 pad 2: GND -> DRDY4
- R40 pad 1: Net-(D16-A) -> +3.3V
- R40 pad 2: +5V -> Net-(U8-RESET)
- R41 pad 1: PT_READING_1 -> PT_READ_4
- R41 pad 2: GND -> /ADC2/AIN3
- R42 pad 1: PT_READING_4 -> PT_READ_3
- R42 pad 2: GND -> /ADC2/AIN2
- R43 pad 1: PT_READING_2 -> PT_READ_2
- R43 pad 2: GND -> /ADC2/AIN1
- R44 pad 1: PT_READING_5 -> PT_READ_1
- R44 pad 2: GND -> /ADC2/AIN0
- R45 pad 1: PT_READING_3 -> +3.3V
- R45 pad 2: GND -> Net-(U9-RESET)
- R46 pad 1: PT_READING_6 -> +3.3V
- R46 pad 2: GND -> Net-(U10-RESET)
- R49 pad 1: Net-(U8--) -> TC2+
- R49 pad 2: /Ignitor Control/IGNITOR_+VE -> +5V
- R5 pad 1: Net-(J3-CC2) -> +3.3V
- R5 pad 2: GND -> DRDY5
- R50 pad 1: Net-(D19-A) -> GND
- R50 pad 2: /Ignitor Control/IGN_SUPPLY -> TC2-
- R51 pad 1: /Ignitor Control/IGNITOR_CTL_FET -> TC1+
- R51 pad 2: GND -> /ThermocoupleADC1/AIN3
- R52 pad 1: /Ignitor Control/IGNITOR_CTL_FET -> TC1-
- R52 pad 2: IGNITOR_CTL -> /ThermocoupleADC1/AIN2
- R53 pad 1: +5V -> TC2+
- R53 pad 2: GND -> /ThermocoupleADC1/AIN1
- R54 pad 1: IGN_Current_Measurement -> TC2-
- R54 pad 2: ADC1_AIN3 -> /ThermocoupleADC1/AIN0
- R55 pad 1: Net-(J21-Pin_3) -> +3.3V
- R55 pad 2: ADC1_AIN2 -> Net-(U11-RESET)
- R56 pad 1: Net-(J21-Pin_2) -> TC3+
- R56 pad 2: ADC1_AIN1 -> +5V
- R57 pad 1: Net-(J21-Pin_1) -> GND
- R57 pad 2: ADC1_AIN0 -> TC3-
- R58 pad 1: Net-(J22-Pin_2) -> TC4+
- R58 pad 2: ADC2_AIN3 -> +5V
- R59 pad 1: Net-(J22-Pin_1) -> GND
- R59 pad 2: ADC2_AIN2 -> TC4-
- R6 pad 1: Net-(D1-A) -> I2C_SDA
- R6 pad 2: WIFI_IND -> +3.3V
- R60 pad 1: LC_FILL_+ -> TC3+
- R60 pad 2: ADC2_AIN1 -> /ThermocoupleADC2/AIN3
- R61 pad 1: LC_FILL_- -> TC3-
- R61 pad 2: ADC2_AIN0 -> /ThermocoupleADC2/AIN2
- R62 pad 1: LC_THRUST_+ -> TC4+
- R62 pad 2: ADC3_AIN3 -> /ThermocoupleADC2/AIN1
- R63 pad 1: LC_THRUST_- -> TC4-
- R63 pad 2: ADC3_AIN2 -> /ThermocoupleADC2/AIN0
- R64 pad 1: PT_READING_1 -> +24V_PT
- R64 pad 2: ADC3_AIN1 -> Net-(J5-Pin_1)
- R65 pad 1: PT_READING_2 -> +24V_PT
- R65 pad 2: ADC3_AIN0 -> Net-(J6-Pin_1)
- R66 pad 1: PT_READING_3 -> PT_READ_1
- R66 pad 2: ADC4_AIN3 -> GND
- R67 pad 1: PT_READING_4 -> PT_READ_4
- R67 pad 2: ADC4_AIN2 -> GND
- R68 pad 1: PT_READING_5 -> +24V_PT
- R68 pad 2: ADC4_AIN1 -> Net-(J7-Pin_1)
- R69 pad 1: PT_READING_6 -> +24V_PT
- R69 pad 2: ADC4_AIN0 -> Net-(J8-Pin_1)
- R7 pad 1: +24V_SAFE -> I2C_SCL
- R7 pad 2: 24V_SAFE_DETECT -> +3.3V
- R8 pad 1: 24V_SAFE_DETECT -> GND
- R8 pad 2: GND -> Net-(J1-Pin_1)
- R9 pad 1: VALVE_1_CTL -> Net-(D1-A)
- R9 pad 2: Net-(Q1-G) -> /Power Regulation/+24V_POST_LCKT
- SW1 pad 1: RESET -> /ESP32 Breakout/RESET
- SW2 pad 1: BOOT -> /ESP32 Breakout/BOOT
- U1 pad 1: GND -> /Power Regulation/PWR_SQ
- U1 pad 2: +3.3V -> GND
- U1 pad 3: RESET -> Net-(J1-Pin_1)
- U1 pad 4: SAFE_24V_CTL -> Net-(Q2-G)
- U1 pad 5: IGNITOR_CTL -> /Power Regulation/+5V_EN
- U1 pad 6: 24V_SAFE_DETECT -> /Power Regulation/+3.3V_EN
- U2 pad 2: GND -> +24V
- U2 pad 3: Net-(U2-RESET) -> +24V
- U2 pad 4: GND -> BUCK_PG
- U2 pad 5: GND -> Net-(U2-FB)
- U2 pad 6: ADC1_AIN3 -> /Power Regulation/VCC
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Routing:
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- removed copper zone on B.Cu, net GND
- removed copper zone on F.Cu, net GND
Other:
- board size 100 x 125 mm -> 15.8 x 16.2 mm
- board text removed: "+24V"
- board text removed: "+3.3V"
- board text removed: "+5V"
- board text removed: "<-- Beware of exhaust"
- board text removed: "ADC1"
- board text removed: "ADC1 0 1 2"
- board text removed: "ADC2"
- board text removed: "ADC2 2 3"
- board text removed: "ADC3"
- board text removed: "ADC4"
- board text removed: "AVDUMP-42"
- board text removed: "AVFILL-43"
- board text removed: "AVPURGE1-1"
- board text removed: "AVPURGE2-2"
- board text removed: "AVRUN-44"
- board text removed: "AVVENT-41"
- board text removed: "BOOT"
- board text removed: "IGN"
- board text removed: "KEY+24V"
- board text removed: "LCRUN"
- board text removed: "LCTHRUST"
- board text removed: "PANDA Propulsion Actuation and Nominal Data Acquisition V2.0.0 Nov 6th 2025 Noah Warren, Nathan Belza"
- board text removed: "PT1"
- board text removed: "PT2"
- board text removed: "PT3"
- board text removed: "PT4"
- board text removed: "PT5"
- board text removed: "PT6"
- board text removed: "RST"
- board text removed: "SAFE+24V"
- board text removed: "WiFi"
- board text removed: "https://github.com/Queens-Rocket-Engineering-Team/prop-pandaV2"

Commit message: start pcb design
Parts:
- removed R28: 100k, Resistor_SMD:R_0603_1608Metric
- removed U4: TLC555xD, Package_SO:SOIC-8_3.9x4.9mm_P1.27mm
- added U14: TLC555xPS, Package_SO:VSSOP-8_3x3mm_P0.65mm, F.Cu at (217.0, 33.6)
- moved C14 217.5 mm to (220.8, 32.2), turned to -90 degrees
- moved C11 212.3 mm to (217.8, 36.1)
- moved C16 209.4 mm to (220.5, 36.1), turned to 180 degrees
- moved C19 202.7 mm to (212.0, 53.0), turned to 90 degrees
- moved C21 200.3 mm to (208.0, 51.6), turned to -90 degrees
- moved C18 198.1 mm to (208.0, 53.5), turned to 90 degrees
- moved R27 179.8 mm to (221.3, 33.6)
- moved R26 178.4 mm to (221.3, 34.7), turned to 180 degrees
- moved R24 177.8 mm to (215.1, 37.9)
- moved R23 177.6 mm to (215.1, 36.2), turned to 180 degrees
- moved Q1 175.9 mm to (192.6, 39.6)
- moved C61 173.2 mm to (260.3, 54.8)
- moved F2 173.2 mm to (240.0, 49.7)
- moved J13 173.2 mm to (262.1, 38.0)
- moved K2 173.2 mm to (238.6, 32.2)
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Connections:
- R20 pad 2: /Power Regulation/VCC -> +3.3V
- U6 pad 8: Net-(U6-ST) -> unconnected-(U6-ST-Pad8)
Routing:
- net /Power Regulation/+5.3V: track 0.00 -> 30.1 mm, vias 0 -> 2
- net GND: track 0.00 -> 18.4 mm, vias 0 -> 16
- net +24V: track 0.00 -> 9.55 mm
- net /Power Regulation/TR: track 0.00 -> 8.10 mm
- net +24V_PT: track 0.00 -> 6.30 mm
- net /Power Regulation/PWR_SQ: track 0.00 -> 5.47 mm
- net Net-(U14-R): track 0.00 -> 3.66 mm
- net Net-(U14-DIS): track 0.00 -> 3.32 mm
- net Net-(Q3-G): track 0.00 -> 3.13 mm
- net +3.3V: track 0.00 -> 2.67 mm
- net /Power Regulation/VCC: track 0.00 -> 2.10 mm
- net Net-(Q2-D): track 0.00 -> 1.90 mm
- net Net-(U14-CV): track 0.00 -> 1.84 mm
- net Net-(U2-BOOT): track 0.00 -> 1.81 mm
- net Net-(Q2-G): track 0.00 -> 1.71 mm
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- added copper zone on F.Cu, net /Power Regulation/+5.3V
- added copper zone on F.Cu, net /Power Regulation/SW
- added copper zone on F.Cu, net GND
- added copper zone on In1.Cu, net GND
- added copper zone on In2.Cu, net GND
- added copper zone on F.Cu, net Net-(U2-FB)
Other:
- board size 15.8 x 16.2 mm -> 122.9 x 136.7 mm
- copper layers 2 -> 4
